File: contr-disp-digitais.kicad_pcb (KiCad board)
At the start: 2 copper layers, 185 x 64 mm, 77 parts, among them J1 Conn_01x02, J2 Conn_01x06, SW1 SW_SPDT, T1 Transformer_1P_2S, U1 LM7815_TO220, U2 LM7915_TO220, U3 TL081, U4 TL081, U5 TL081, U6 TL081, U7 TL081, U8 TL081

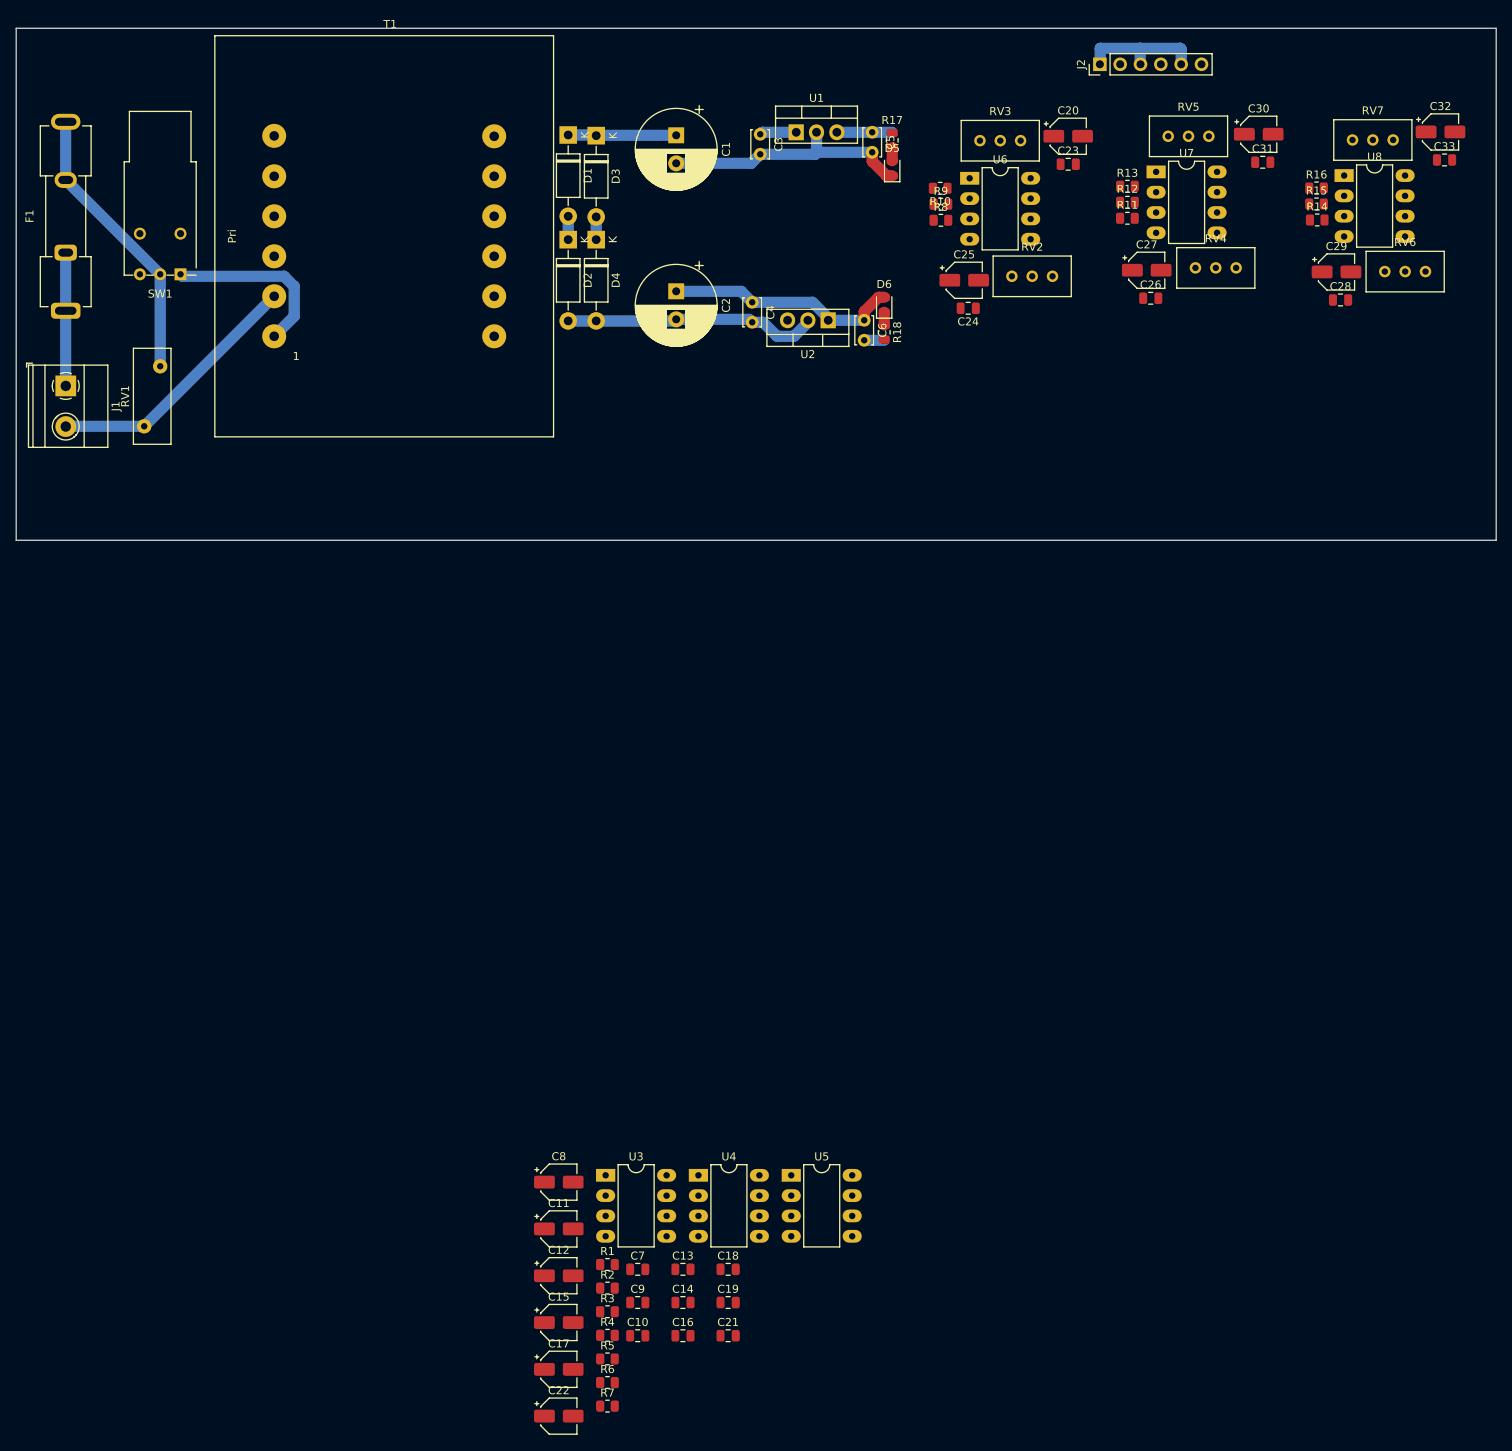
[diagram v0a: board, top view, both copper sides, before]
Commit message: Finalização de posicionamento de componentes no PCB, REVISÃO PENDENTE!!!
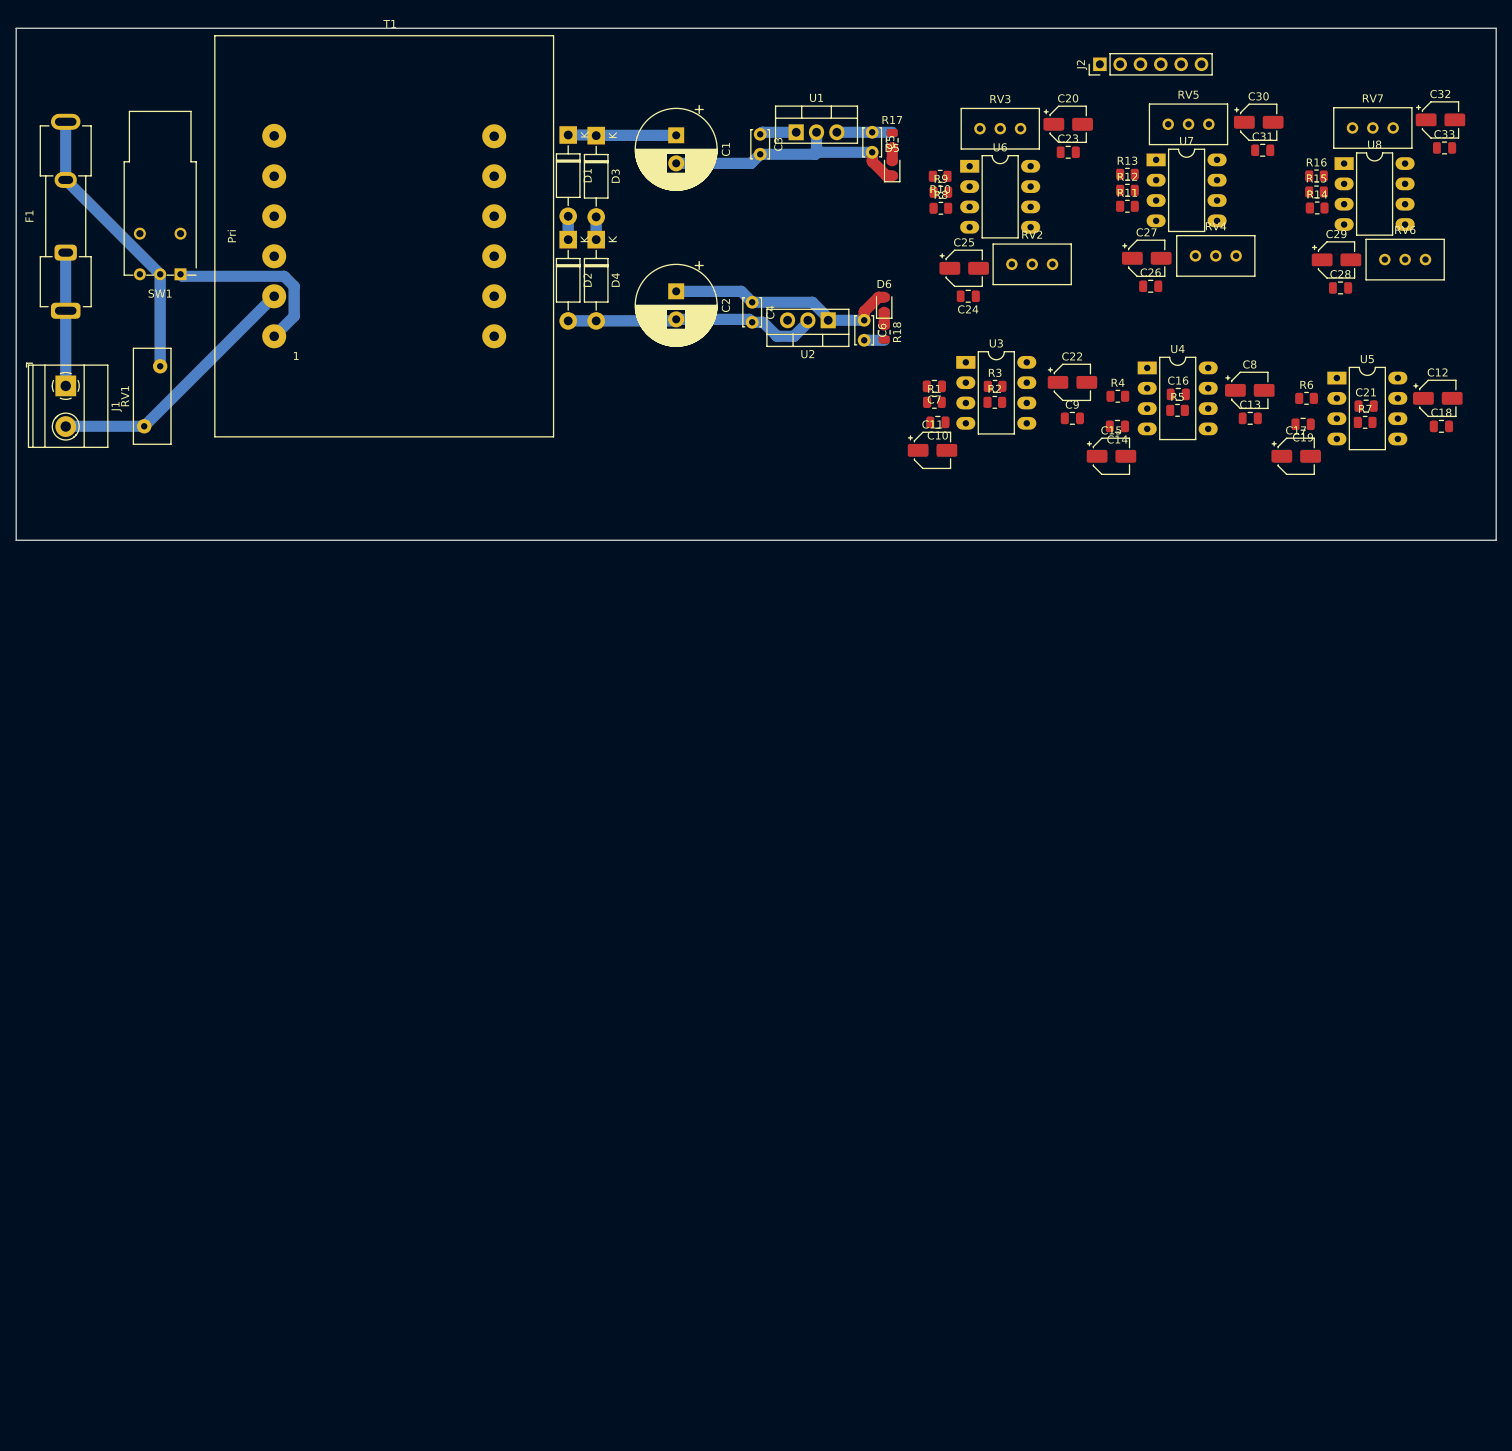
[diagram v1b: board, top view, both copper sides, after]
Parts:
- moved C12 155.2 mm to (189.7, 58.3)
- moved R7 155.2 mm to (180.6, 61.3)
- moved R6 150.9 mm to (173.3, 58.3)
- moved C17 146.7 mm to (172.0, 65.5)
- moved C22 144.3 mm to (144.0, 56.3)
- moved C21 140.9 mm to (180.7, 59.2)
- moved R5 138.3 mm to (157.2, 59.8)
- moved C18 138.0 mm to (190.2, 61.8)
- moved R4 133.6 mm to (149.7, 58.0)
- moved C16 133.0 mm to (157.3, 57.8)
- moved C8 131.4 mm to (166.2, 57.3)
- moved C19 131.2 mm to (172.9, 61.5), turned to 180 degrees
- moved C15 128.4 mm to (148.9, 65.5)
- moved C13 127.8 mm to (166.3, 60.8)
- moved R3 125.4 mm to (134.4, 56.8)
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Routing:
- net GND: track 78.5 -> 62.4 mm

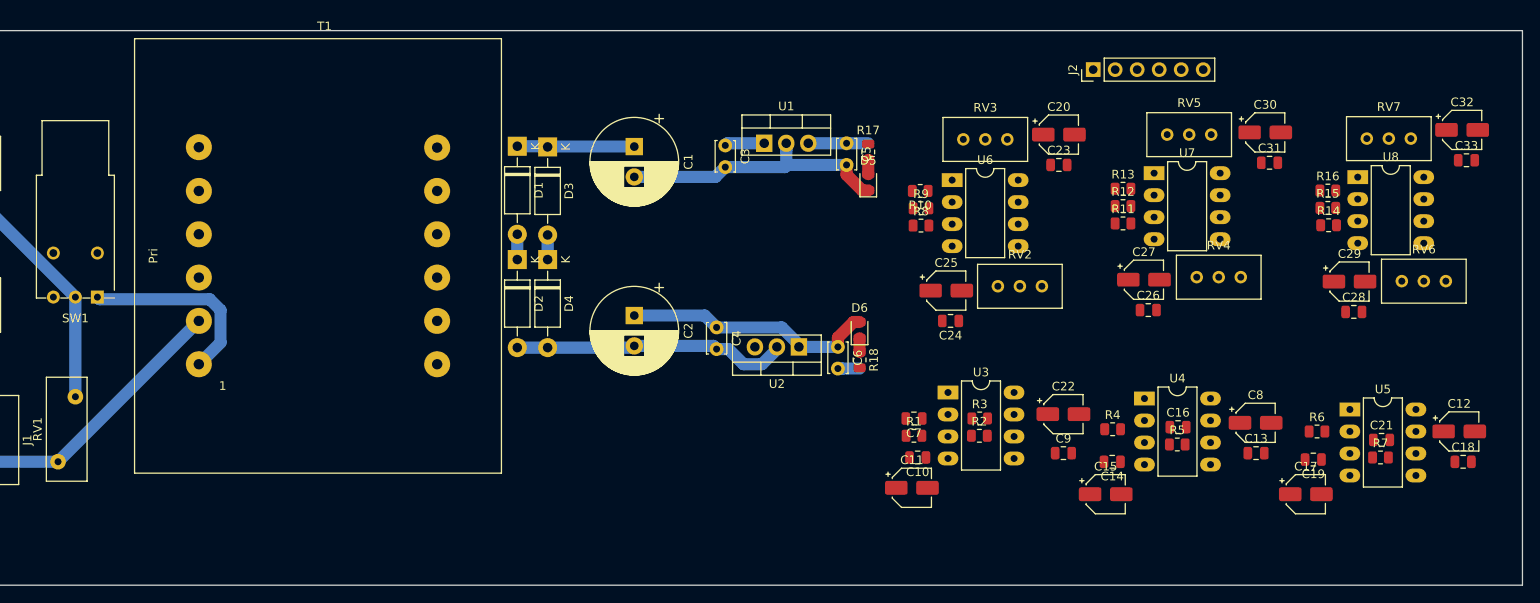
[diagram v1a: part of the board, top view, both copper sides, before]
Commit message: Trilhas de alimentação finalizadas no PCB, alterações futuras possíveis e prováveis.
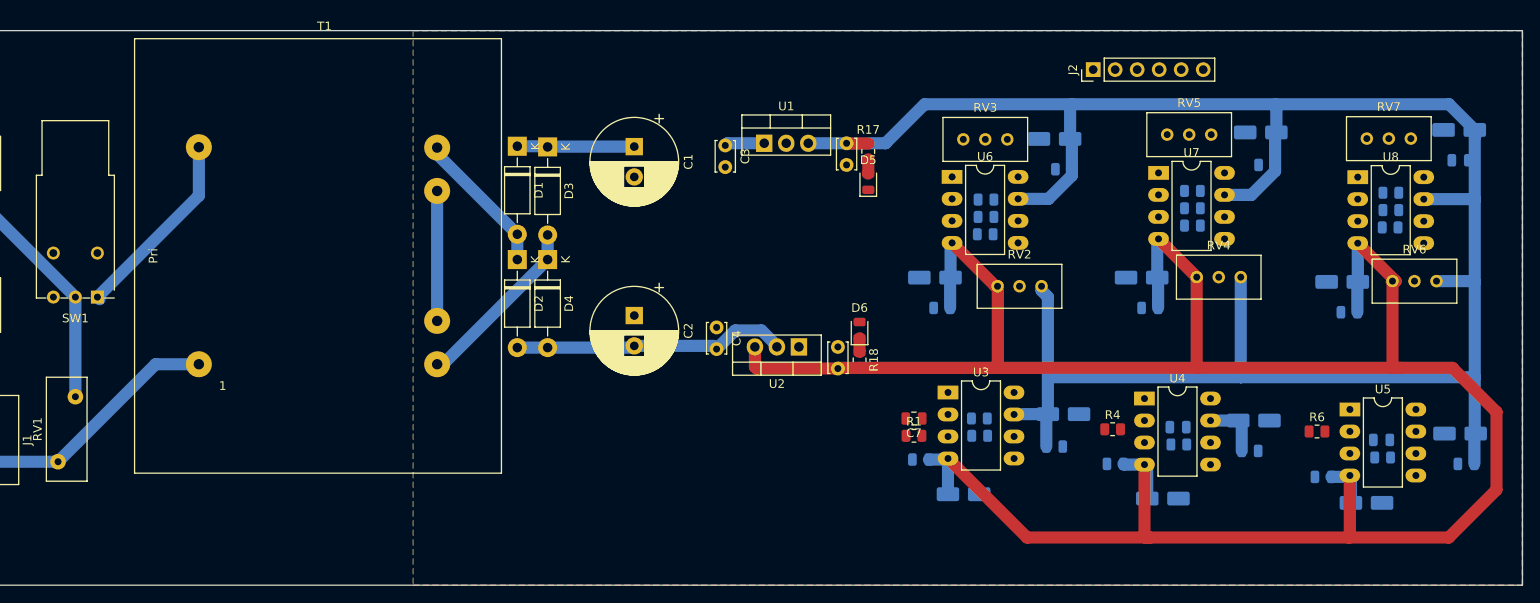
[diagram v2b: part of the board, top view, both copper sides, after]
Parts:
- C10, C11, C12, C13, C14, C15, C16, C17, C18, C19, C20, C21, C22, C23, C24, C25, C26, C27, C28, C29, C30, C31, C32, C33, C8, C9, R10, R11, R12, R13, R14, R15, R16, R2, R3, R5, R7, R8, R9: moved to B.Cu
- moved R10 9.01 mm to (135.0, 35.5), turned to 0 degrees
- moved R8 8.08 mm to (135.1, 31.5), turned to 180 degrees
- moved R11 8.01 mm to (158.9, 34.5), turned to 180 degrees
- moved R12 8.01 mm to (158.9, 32.5), turned to 180 degrees
- moved R13 8.01 mm to (158.9, 30.5)
- moved R9 7.57 mm to (135.1, 33.5), turned to 180 degrees
- moved R15 7.28 mm to (181.8, 32.7), turned to 180 degrees
- moved R16 7.28 mm to (181.8, 30.7)
- moved R14 7.10 mm to (181.7, 34.7), turned to 180 degrees
- moved C17 7.07 mm to (179.0, 66.5), turned to 180 degrees
- moved C15 6.61 mm to (155.5, 66.0), turned to 180 degrees
- moved C11 6.01 mm to (132.5, 65.5), turned to 180 degrees
- moved C19 2.30 mm to (174.0, 63.5)
- moved C25 1.98 mm to (129.2, 40.5)
- moved C24 1.80 mm to (130.0, 44.0)
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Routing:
- net -15V: track 2.50 -> 277.7 mm
- net +15V: track 6.92 -> 252.9 mm
- net GND: track 62.4 -> 15.0 mm
- net Net-(D3-A): track 2.84 -> 20.6 mm
- net Net-(D1-A): track 2.92 -> 16.8 mm
- net Net-(J1-Pin_2): track 32.8 -> 30.7 mm
- added copper zone on B.Cu, net GND
- added copper zone on F.Cu, net GND

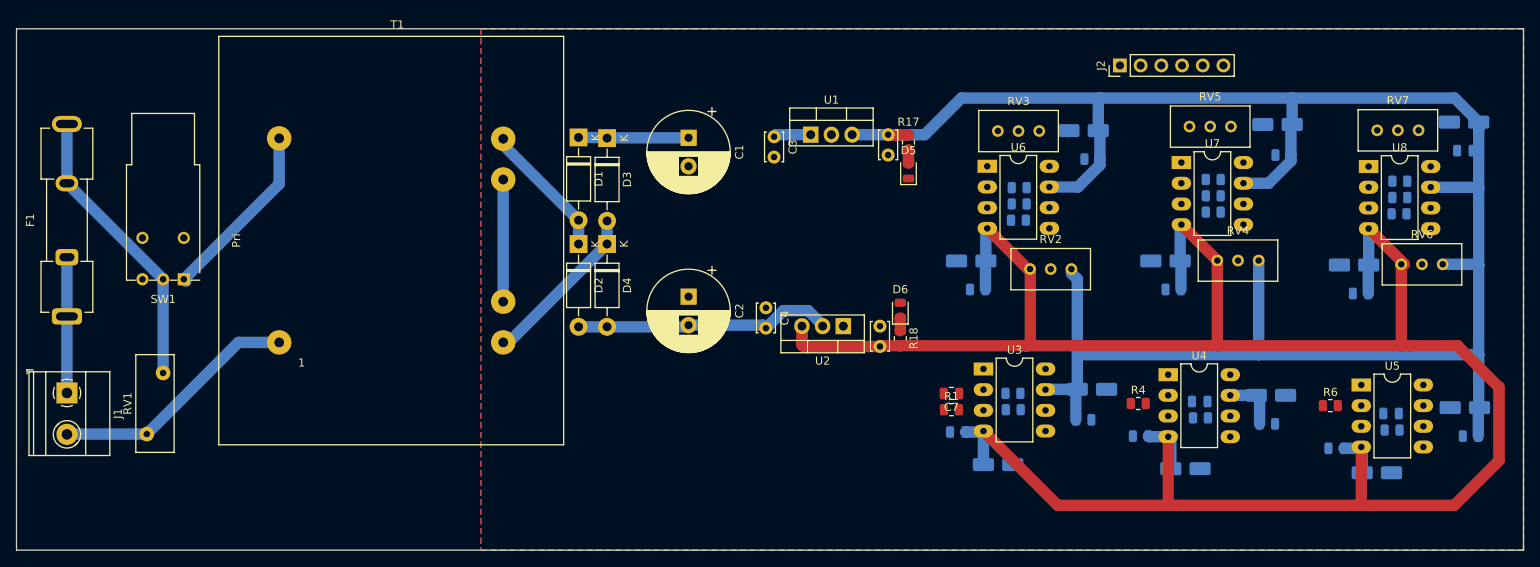
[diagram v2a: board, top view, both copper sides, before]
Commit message: Todas as trilhas finalizadas. Faltando para finalizar somente consertar 3 erros que remanescem, revisar e fazer melhorias possíveis até o dia da entrega.
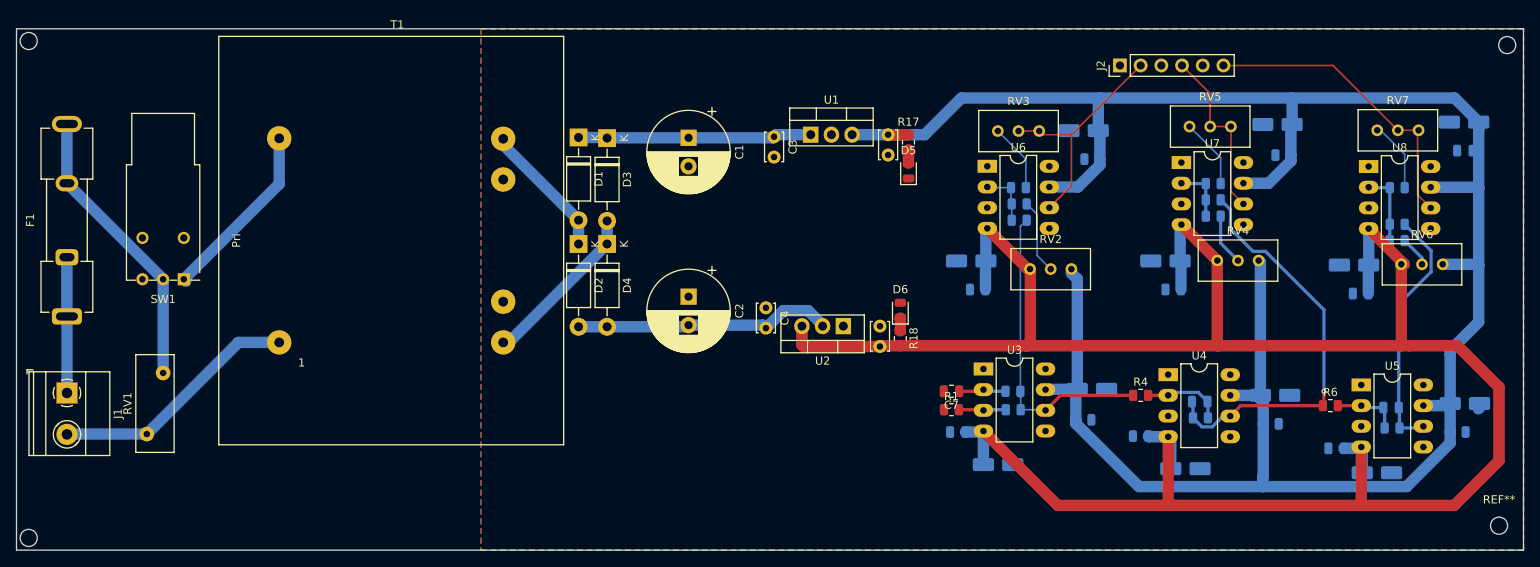
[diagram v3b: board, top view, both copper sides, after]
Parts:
- added ?: , , F.Cu at (195.0, 14.0)
- added ?: , , F.Cu at (13.5, 13.5)
- added ?: , , F.Cu at (13.5, 74.5)
- added REF**: MountingHole_2.1mm, MountingHole:MountingHole_2.1mm, F.Cu at (194.0, 73.0)
- moved R10 4.00 mm to (135.0, 31.5)
- moved R15 3.31 mm to (181.5, 36.0)
- moved R14 3.30 mm to (181.5, 38.0)
- moved R8 2.00 mm to (135.1, 33.5)
- moved R9 2.00 mm to (135.1, 35.5)
- moved C18 1.63 mm to (188.9, 61.5), turned to 0 degrees
- moved R4 1.04 mm to (150.0, 57.0)
- moved R16 0.85 mm to (181.5, 31.5)
- moved C21 0.73 mm to (180.7, 58.5), turned to 0 degrees
- moved C12 0.50 mm to (189.8, 58.0), turned to 0 degrees
- moved C8 0.50 mm to (166.5, 57.0)
- moved R11 0.50 mm to (158.9, 35.0)
- moved R12 0.50 mm to (158.9, 33.0)
- moved R13 0.50 mm to (158.9, 31.0)
- moved C13 0.45 mm to (166.0, 60.5)
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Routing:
- net Triangular_1: track 0.00 -> 51.0 mm, vias 0 -> 1
- net Quadrada_1: track 0.00 -> 38.2 mm
- net Senoidal: track 0.00 -> 37.5 mm
- net Senoidal_1: track 0.00 -> 31.0 mm
- net Quadrada: track 0.00 -> 28.8 mm
- net +15V: track 252.9 -> 275.6 mm
- net Triangular: track 0.00 -> 21.6 mm
- net GND: track 15.0 -> 0.35 mm
- net Net-(D1-K): track 18.2 -> 28.7 mm
- net Net-(U4--): track 0.00 -> 9.93 mm
- net Net-(R8-Pad1): track 0.00 -> 9.23 mm
- net Net-(U8--): track 0.00 -> 9.12 mm
- net Net-(R16-Pad2): track 0.00 -> 8.68 mm
- net Net-(R10-Pad2): track 0.00 -> 8.38 mm
- net Net-(U5--): track 0.00 -> 8.25 mm
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
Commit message: Erros tratados e furações de suporte incluídos. Remanesce somente a revisão geral para a entrega.
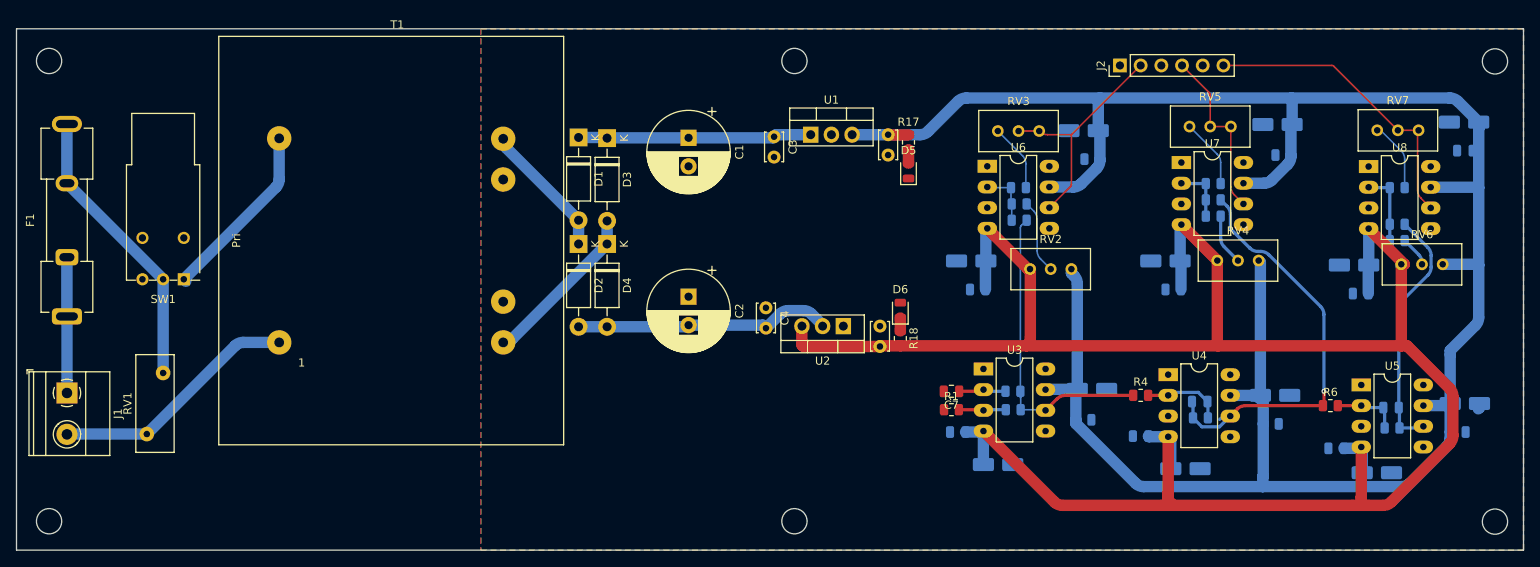
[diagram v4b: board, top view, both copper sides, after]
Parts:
- removed ? (x3): , 
- removed REF**: MountingHole_2.1mm, MountingHole:MountingHole_2.1mm
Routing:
- net -15V: track 277.7 -> 266.1 mm
- net Triangular_1: track 51.0 -> 52.1 mm
- net +15V: track 275.6 -> 274.8 mm
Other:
- outline, holes or cut-outs redrawn
